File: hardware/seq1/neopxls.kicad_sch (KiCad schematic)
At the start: 13 parts

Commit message: schematic and layout for v1 board
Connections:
- no-connect marks 0 -> 1
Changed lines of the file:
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@@
 		(color 0 0 0 0)
 	)
+	(no_connect
+		(at 224.79 111.76)
+	)
 	(wire
 		(pts
@@
 		)
 	)
-	(label "NPXL_D5V"
-		(at 58.42 111.76 0)
+	(global_label "NPXL_D5V"
+		(shape input)
+		(at 58.42 111.76 180)
 		(fields_autoplaced yes)
 		(effects
@@
 				(size 1.27 1.27)
 			)
-			(justify left bottom)
-		)
-	)
+			(justify right)
+		)
+		(property "Intersheetrefs" "${INTERSHEET_REFS}"
+			(at 46.061 111.76 0)
+			(effects
+				(font
+					(size 1.27 1.27)
+				)
+				(justify right)
+				(hide yes)
+			)
+		)
+	)

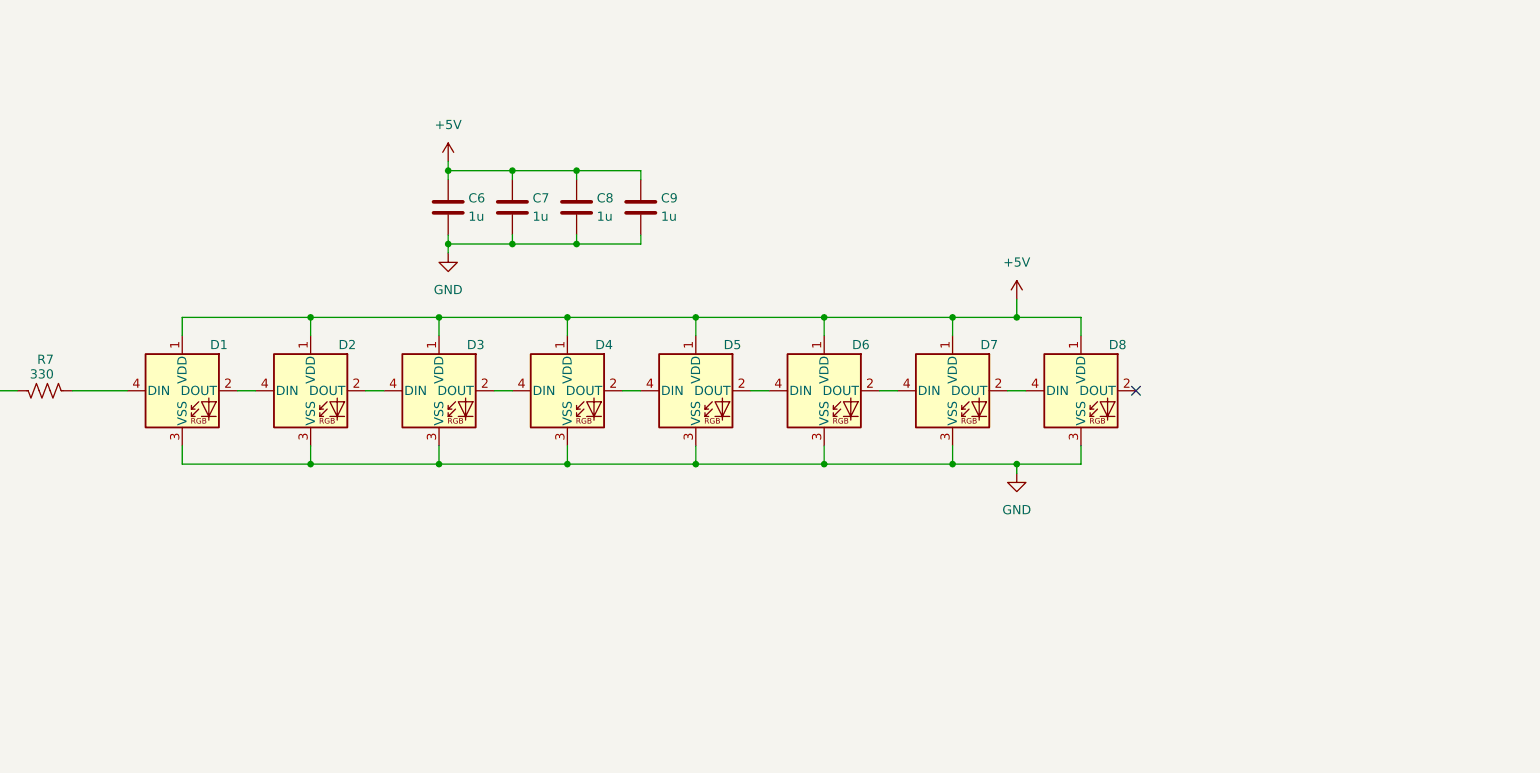
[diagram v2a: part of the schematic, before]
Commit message: updating the board with new line in
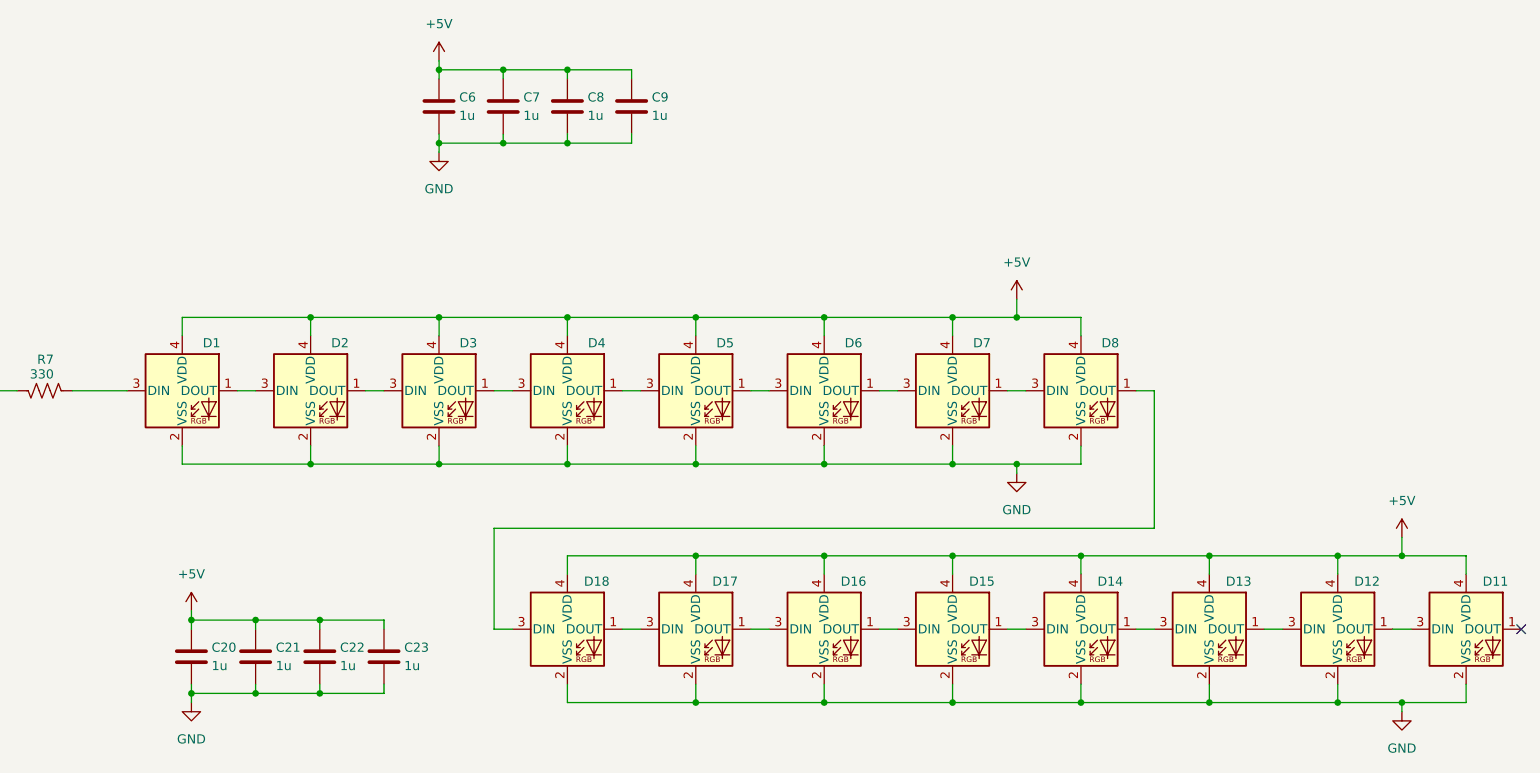
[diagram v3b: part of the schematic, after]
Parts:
- removed D1, D2, D3, D4, D5, D6, D7, D8: WS2812B, LED_SMD:LED_WS2812B_PLCC4_5.0x5.0mm_P3.2mm, symbol LED:WS2812B
- added C20, C21, C22, C23: 1u, Capacitor_THT:C_Disc_D5.0mm_W2.5mm_P5.00mm, symbol Device:C
- added D1, D11, D12, D13, D14, D15, D16, D17, D18, D2, D3, D4, D5, D6, D7, D8: SK6805, LED_SMD:LED_SK6805_PLCC4_2.4x2.7mm_P1.3mm, symbol LED:SK6805
- C6, C7, C8, C9: footprint Capacitor_THT:C_Disc_D5.0mm_W2.5mm_P5.00mm -> Capacitor_THT:C_Disc_D5.0mm_W2.5mm_P2.50mm
- R7: footprint Resistor_THT:R_Axial_DIN0207_L6.3mm_D2.5mm_P2.54mm_Vertical -> Resistor_THT:R_Axial_DIN0204_L3.6mm_D1.6mm_P2.54mm_Vertical
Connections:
- net +5V: now also C20.1, C21.1, C22.1, C23.1, D1.4 (VDD), D11.4 (VDD), D12.4 (VDD), D13.4 (VDD), D14.4 (VDD), D15.4 (VDD), D16.4 (VDD), D17.4 (VDD), D18.4 (VDD), D2.4 (VDD), D3.4 (VDD), D4.4 (VDD), D5.4 (VDD), D6.4 (VDD), D7.4 (VDD), D8.4 (VDD)
- net GND: now also C20.2, C21.2, C22.2, C23.2, D1.2 (VSS), D11.2 (VSS), D12.2 (VSS), D13.2 (VSS), D14.2 (VSS), D15.2 (VSS), D16.2 (VSS), D17.2 (VSS), D18.2 (VSS), D2.2 (VSS), D3.2 (VSS), D4.2 (VSS), D5.2 (VSS), D6.2 (VSS), D7.2 (VSS), D8.2 (VSS)
- net at R7.2: now also D1.3 (DIN)
- new net: D15.3 (DIN), D16.1 (DOUT)
- new net: D16.3 (DIN), D17.1 (DOUT)
- new net: D6.1 (DOUT), D7.3 (DIN)
- new net: D5.1 (DOUT), D6.3 (DIN)
- new net: D3.1 (DOUT), D4.3 (DIN)
- new net: D2.1 (DOUT), D3.3 (DIN)
- new net: D13.3 (DIN), D14.1 (DOUT)
- new net: D14.3 (DIN), D15.1 (DOUT)
- new net: D7.1 (DOUT), D8.3 (DIN)
- new net: D11.3 (DIN), D12.1 (DOUT)
- new net: D12.3 (DIN), D13.1 (DOUT)
- new net: D4.1 (DOUT), D5.3 (DIN)
- new net: D17.3 (DIN), D18.1 (DOUT)
- new net: D18.3 (DIN), D8.1 (DOUT)
- new net: D1.1 (DOUT), D2.3 (DIN)
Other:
- company: (none) -> idyllm
- title: (none) -> Sequencer
- moved on the sheet: C6, C7, C8, C9

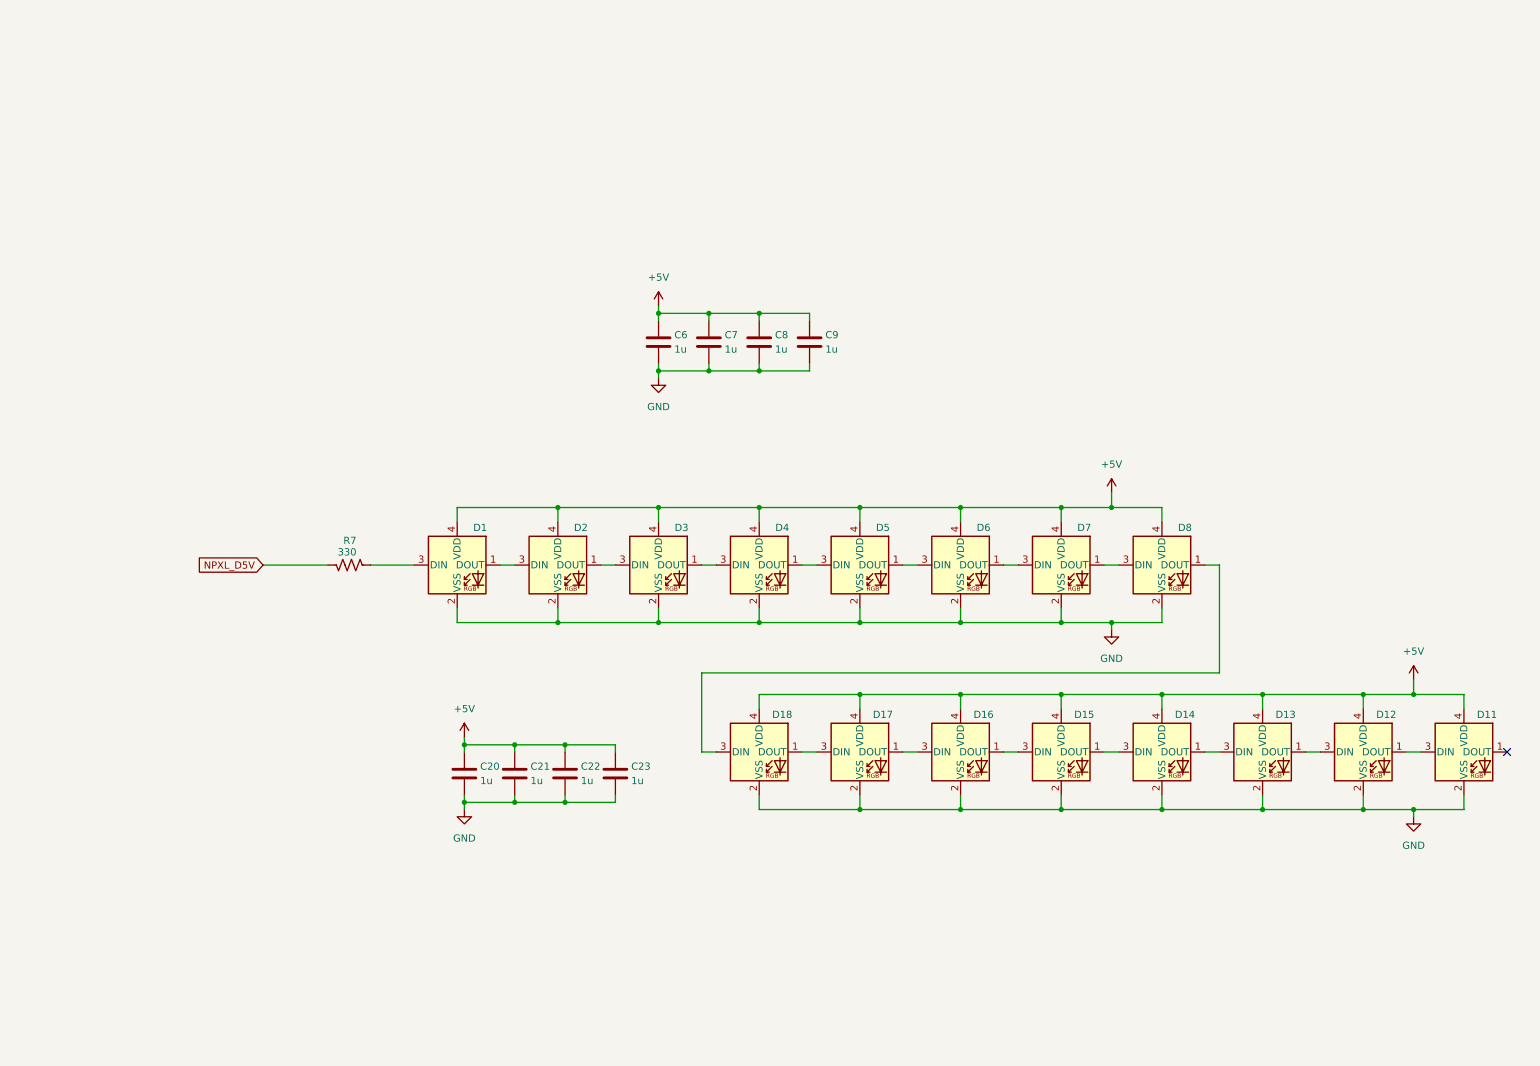
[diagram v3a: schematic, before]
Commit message: layout for v2 board (WIP) with risers part of same schematic/PBC
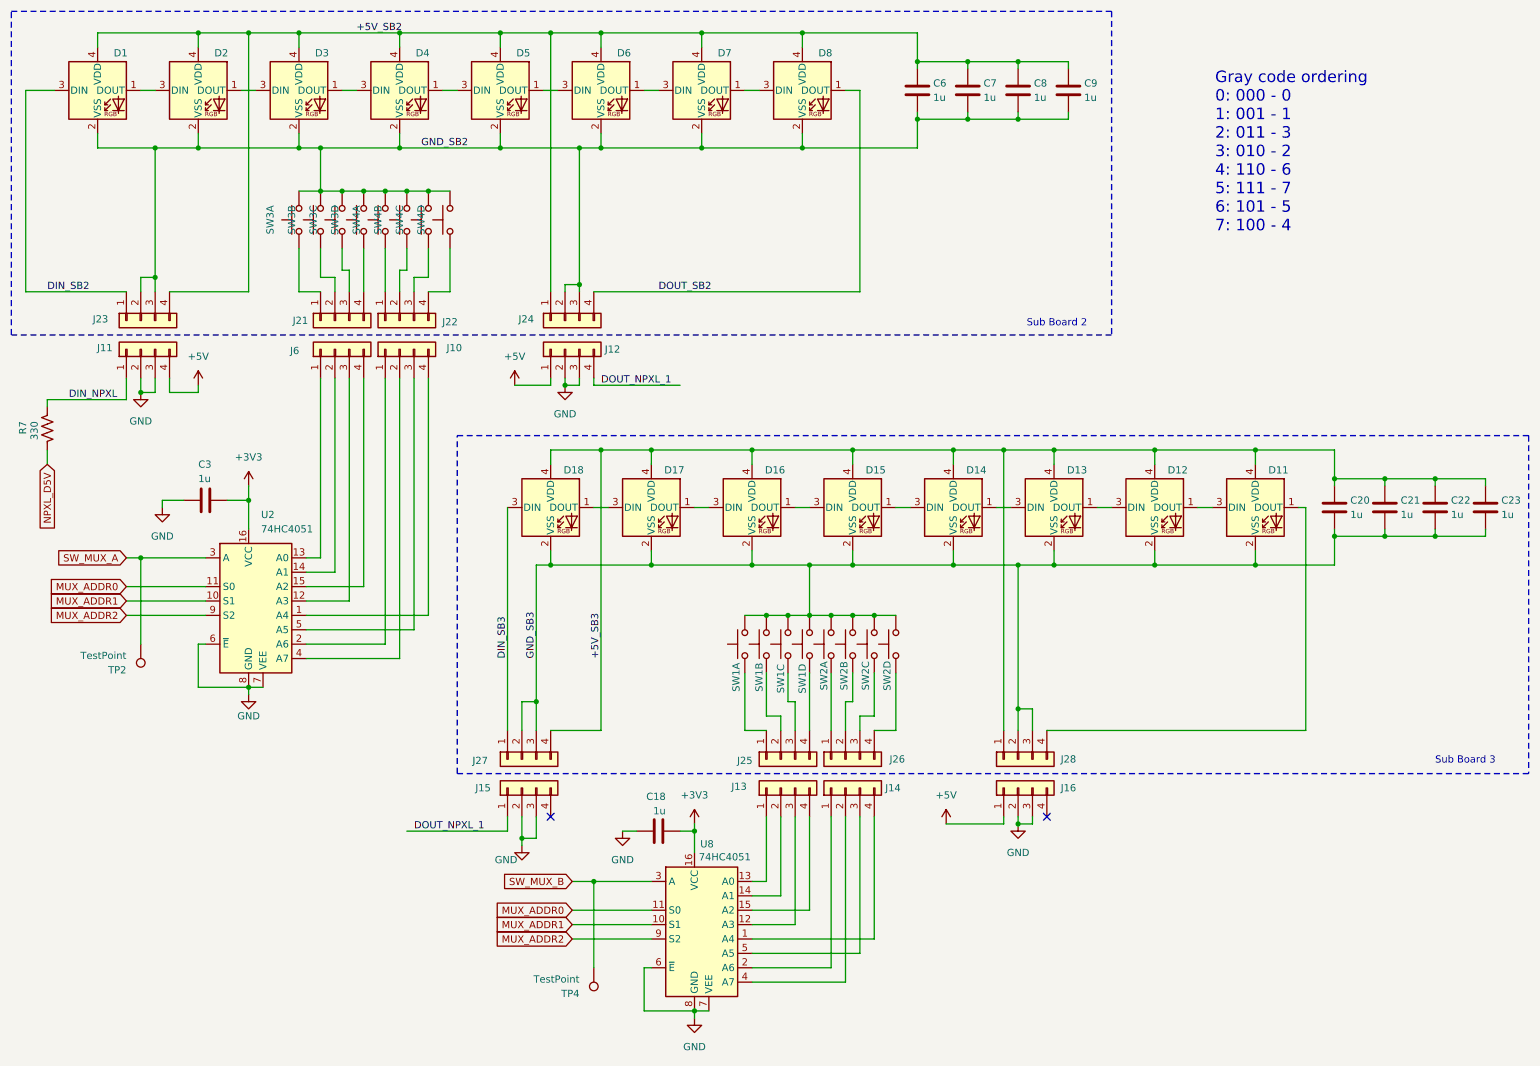
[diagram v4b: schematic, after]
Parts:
- added C18, C3: 1u, Capacitor_THT:C_Disc_D5.0mm_W2.5mm_P2.50mm, symbol Device:C
- added J10, J11, J12, J13, J14, J15, J16, J21, J22, J23, J24, J25, J26, J27, J28, J6: Conn_01x04, Connector_PinHeader_2.54mm:PinHeader_1x04_P2.54mm_Vertical, symbol Connector_Generic:Conn_01x04
- added SW1, SW2, SW3, SW4: SW_Push_x4, Adafruit_Trellis:SW_Silicone_Keypad_PushButton_10mm_4x1grid_NH, symbol Adafruit_Trellis:SW_Push_x4
- added TP2, TP4: TestPoint, Connector_PinHeader_2.54mm:PinHeader_1x01_P2.54mm_Vertical, symbol Connector:TestPoint
- added U2, U8: 74HC4051, Package_DIP:DIP-16_W7.62mm_Socket, symbol 74xx:74HC4051
- C6, C7, C8, C9: footprint Capacitor_THT:C_Disc_D5.0mm_W2.5mm_P2.50mm -> Capacitor_THT:C_Disc_D5.0mm_W2.5mm_P5.00mm
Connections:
- net +5V: now also J11.4 (Pin_4), J12.1 (Pin_1), J16.1 (Pin_1); no longer C20.1, C21.1, C22.1, C23.1, C6.1, C7.1, C8.1, C9.1, D1.4 (VDD), D11.4 (VDD), D12.4 (VDD), D13.4 (VDD), D14.4 (VDD), D15.4 (VDD), D16.4 (VDD), D17.4 (VDD), D18.4 (VDD), D2.4 (VDD), D3.4 (VDD), D4.4 (VDD), D5.4 (VDD), D6.4 (VDD), D7.4 (VDD), D8.4 (VDD)
- net GND: now also C18.1, C3.2, J11.2 (Pin_2), J11.3 (Pin_3), J12.2 (Pin_2), J12.3 (Pin_3), J15.2 (Pin_2), J15.3 (Pin_3), J16.2 (Pin_2), J16.3 (Pin_3), U2.6 (~{E}), U2.7 (VEE), U2.8 (GND), U8.6 (~{E}), U8.7 (VEE), U8.8 (GND); no longer C20.2, C21.2, C22.2, C23.2, C6.2, C7.2, C8.2, C9.2, D1.2 (VSS), D11.2 (VSS), D12.2 (VSS), D13.2 (VSS), D14.2 (VSS), D15.2 (VSS), D16.2 (VSS), D17.2 (VSS), D18.2 (VSS), D2.2 (VSS), D3.2 (VSS), D4.2 (VSS), D5.2 (VSS), D6.2 (VSS), D7.2 (VSS), D8.2 (VSS)
- net DIN_NPXL: now reaches R7.2
- net DIN_NPXL: now also J11.1 (Pin_1); no longer D1.3 (DIN)
- net DIN_SB3: now reaches D18.3 (DIN)
- net DIN_SB3: now also J27.1 (Pin_1); no longer D8.1 (DOUT)
- net at D11.1 (DOUT): now also J28.4 (Pin_4)
- new net: J13.1 (Pin_1), U8.13 (A0)
- new net: J13.2 (Pin_2), U8.14 (A1)
- new net: J13.3 (Pin_3), U8.12 (A3)
- new net: J13.4 (Pin_4), U8.15 (A2)
- new net: J26.1 (Pin_1), SW2.2
- new net: J26.2 (Pin_2), SW2.4
- new net: J26.3 (Pin_3), SW2.6
- new net: J26.4 (Pin_4), SW2.8
- new net: J21.4 (Pin_4), SW3.8
- new net: J25.2 (Pin_2), SW1.4
- new net: J21.1 (Pin_1), SW3.2
- new net: J22.2 (Pin_2), SW4.4
- new net: J22.1 (Pin_1), SW4.2
- new net: J22.3 (Pin_3), SW4.6
- new net: J22.4 (Pin_4), SW4.8
- new net: J25.1 (Pin_1), SW1.2
- new net: J25.3 (Pin_3), SW1.6
- new net: J25.4 (Pin_4), SW1.8
- new net: J21.3 (Pin_3), SW3.6
- new net: J10.4 (Pin_4), U2.1 (A4)
- new net: J6.3 (Pin_3), U2.12 (A3)
- new net: J6.1 (Pin_1), U2.13 (A0)
- new net: J6.2 (Pin_2), U2.14 (A1)
- new net: J6.4 (Pin_4), U2.15 (A2)
- new net: J10.1 (Pin_1), U2.2 (A6)
- new net: J10.2 (Pin_2), U2.4 (A7)
- new net: J10.3 (Pin_3), U2.5 (A5)
- new net: J14.1 (Pin_1), U8.2 (A6)
- new net: J14.2 (Pin_2), U8.4 (A7)
- new net: J14.3 (Pin_3), U8.5 (A5)
- new net: J14.4 (Pin_4), U8.1 (A4)
- new net: J21.2 (Pin_2), SW3.4
- new net +3V3: C18.2, C3.1, U2.16 (VCC), U8.16 (VCC)
- new net +5V_SB2: C6.1, C7.1, C8.1, C9.1, D1.4 (VDD), D2.4 (VDD), D3.4 (VDD), D4.4 (VDD), D5.4 (VDD), D6.4 (VDD), D7.4 (VDD), D8.4 (VDD), J23.4 (Pin_4), J24.1 (Pin_1)
- new net +5V_SB3: C20.1, C21.1, C22.1, C23.1, D11.4 (VDD), D12.4 (VDD), D13.4 (VDD), D14.4 (VDD), D15.4 (VDD), D16.4 (VDD), D17.4 (VDD), D18.4 (VDD), J27.4 (Pin_4), J28.1 (Pin_1)
- new net DIN_SB2: D1.3 (DIN), J23.1 (Pin_1)
- new net DOUT_NPXL_1: J12.4 (Pin_4), J15.1 (Pin_1)
- new net DOUT_SB2: D8.1 (DOUT), J24.4 (Pin_4)
- new net GND_SB2: C6.2, C7.2, C8.2, C9.2, D1.2 (VSS), D2.2 (VSS), D3.2 (VSS), D4.2 (VSS), D5.2 (VSS), D6.2 (VSS), D7.2 (VSS), D8.2 (VSS), J23.2 (Pin_2), J23.3 (Pin_3), J24.2 (Pin_2), J24.3 (Pin_3), SW3.1, SW3.3, SW3.5, SW3.7, SW4.1, SW4.3, SW4.5, SW4.7
- new net GND_SB3: C20.2, C21.2, C22.2, C23.2, D11.2 (VSS), D12.2 (VSS), D13.2 (VSS), D14.2 (VSS), D15.2 (VSS), D16.2 (VSS), D17.2 (VSS), D18.2 (VSS), J27.2 (Pin_2), J27.3 (Pin_3), J28.2 (Pin_2), J28.3 (Pin_3), SW1.1, SW1.3, SW1.5, SW1.7, SW2.1, SW2.3, SW2.5, SW2.7
- new net MUX_ADDR0: U2.11 (S0), U8.11 (S0)
- new net MUX_ADDR1: U2.10 (S1), U8.10 (S1)
- new net MUX_ADDR2: U2.9 (S2), U8.9 (S2)
- new net SW_MUX_A: TP2.1, U2.3 (A)
- new net SW_MUX_B: TP4.1, U8.3 (A)
- no-connect marks 1 -> 2
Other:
- note added: "Gray code ordering 0: 000 - 0 1: 001 - 1 2: 011 - 3 3: 010 - 2 4: 110 - 6 5: 111 - 7 6: 101 - 5 7: 100 - 4"
- note added: "Sub Board 2"
- note added: "Sub Board 3"
- moved on the sheet: C20, C21, C22, C23, C6, C7, C8, C9, D11, D12, D13, D14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
